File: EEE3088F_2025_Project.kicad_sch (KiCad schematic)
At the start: 1 part, among them U1 14528

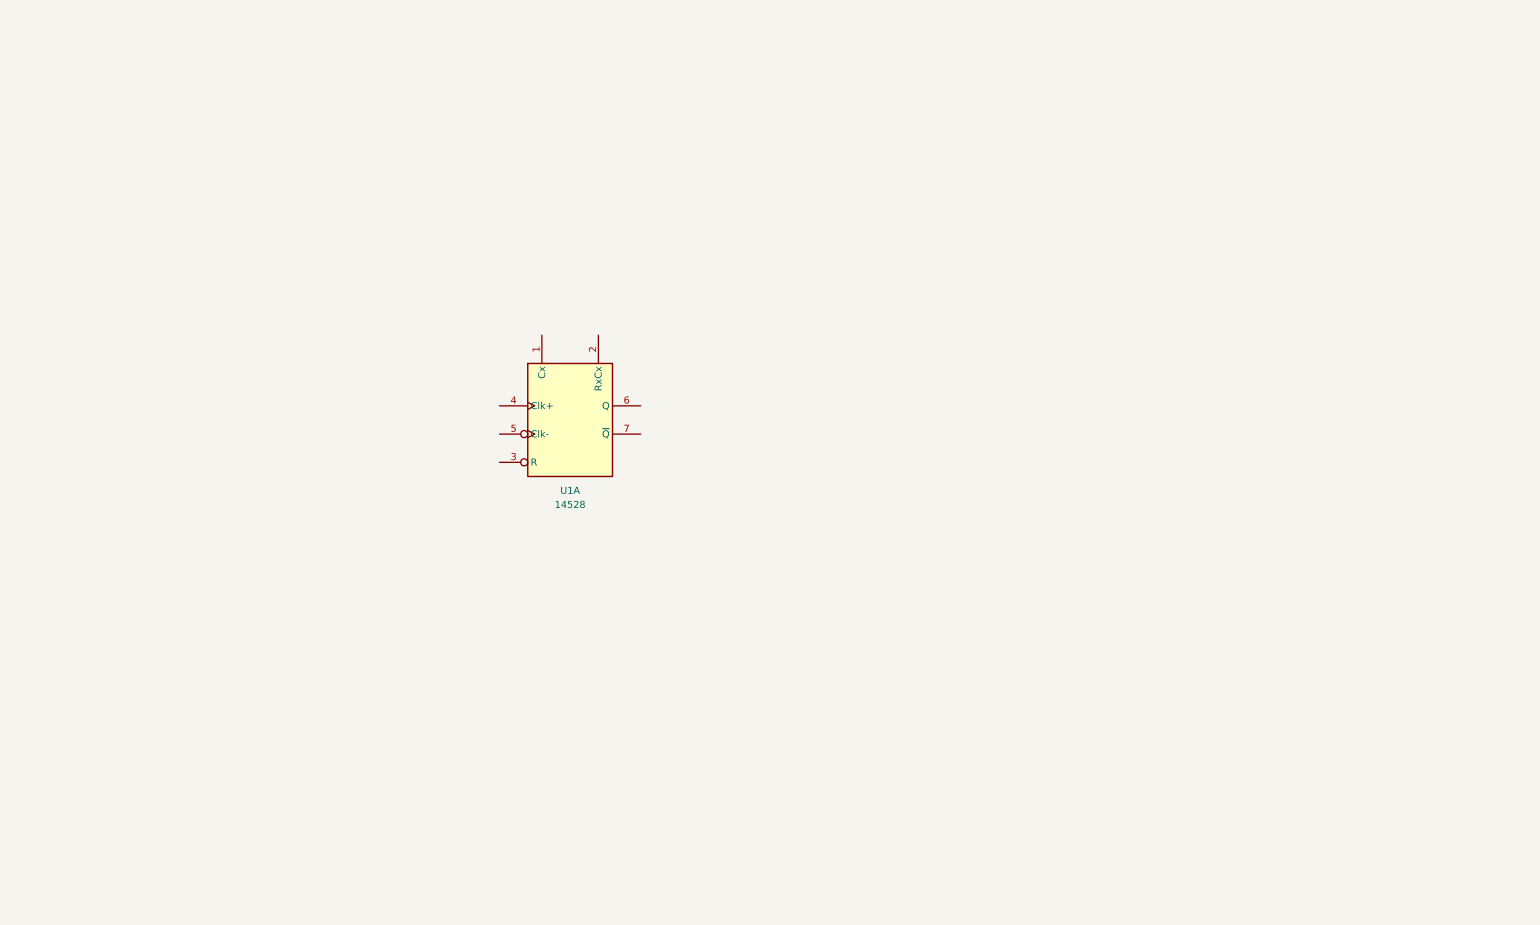
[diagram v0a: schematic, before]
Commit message: Addded motor drivers and connector
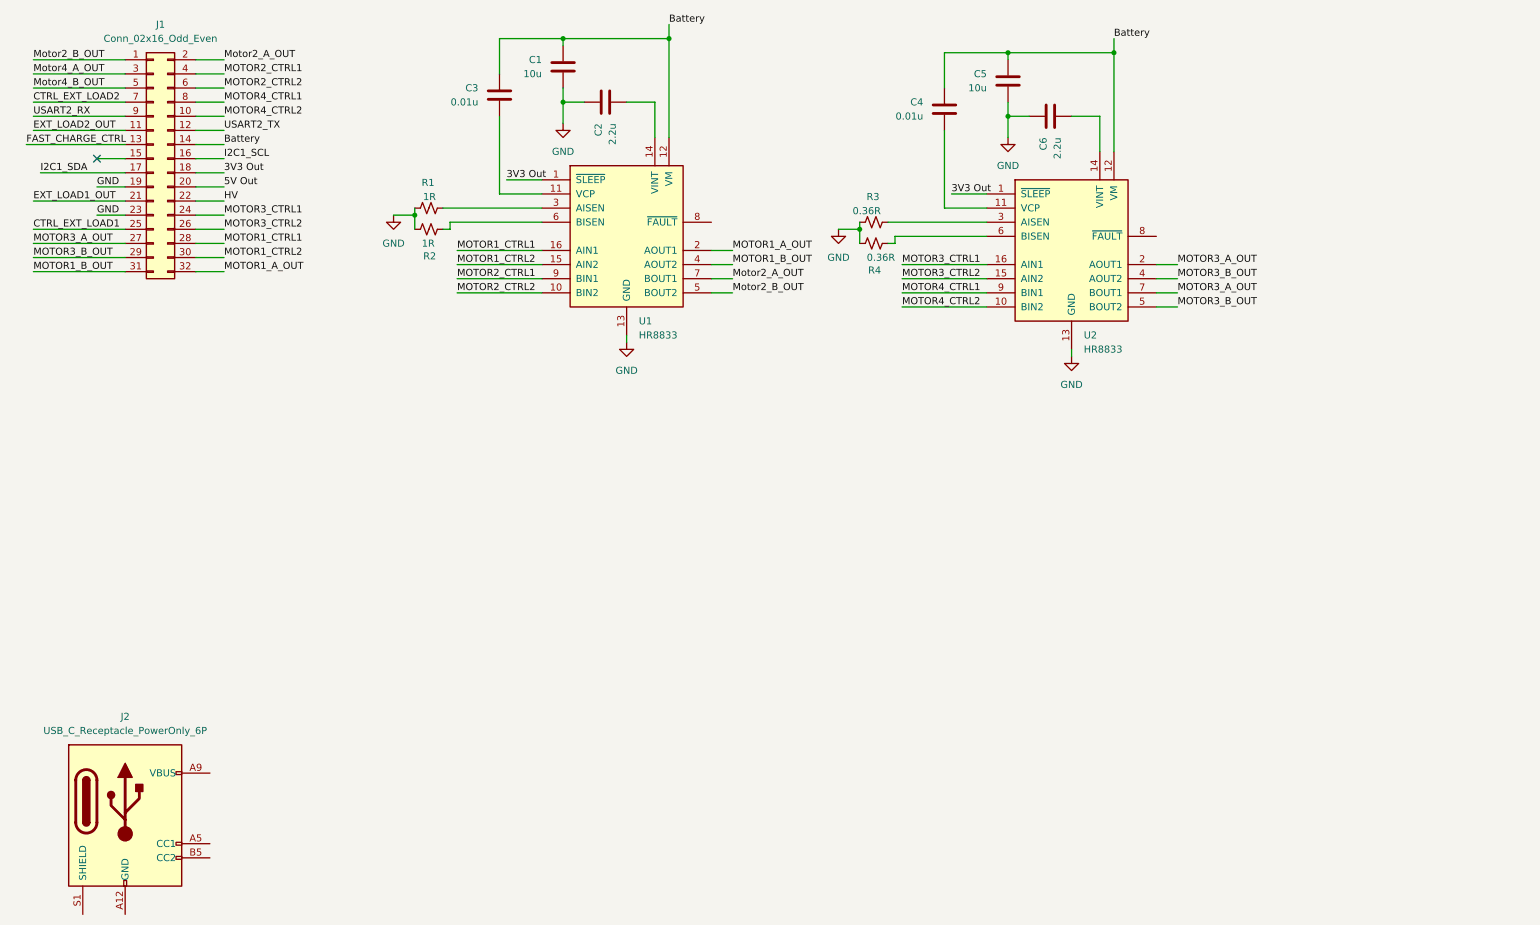
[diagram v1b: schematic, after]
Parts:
- removed U1: 14528, symbol 4xxx:14528
- added C1, C5: 10u, symbol Device:C
- added C2, C6: 2.2u, symbol Device:C
- added C3, C4: 0.01u, symbol Device:C
- added J1: Conn_02x16_Odd_Even, symbol Connector_Generic:Conn_02x16_Odd_Even
- added J2: USB_C_Receptacle_PowerOnly_6P, symbol Connector:USB_C_Receptacle_PowerOnly_6P
- added R1, R2: 1R, symbol Device:R_Small_US
- added R3, R4: 0.36R, symbol Device:R_Small_US
- added U1, U2: HR8833, Package_SO:TSSOP-16-1EP_4.4x5mm_P0.65mm_EP3x3mm, symbol Driver_Motor:DRV8833PW
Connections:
- new net: R2.2, U1.6 (BISEN)
- new net: C6.2, U2.14 (VINT)
- new net: J2.A12 (GND), J2.B12 (GND)
- new net: J2.A9 (VBUS), J2.B9 (VBUS)
- new net: C3.2, U1.11 (VCP)
- new net: C2.2, U1.14 (VINT)
- new net: R1.2, U1.3 (AISEN)
- new net: C4.2, U2.11 (VCP)
- new net: R3.2, U2.3 (AISEN)
- new net: R4.2, U2.6 (BISEN)
- new net 3V3 Out: J1.18 (Pin_18), U1.1 (~{SLEEP}), U2.1 (~{SLEEP})
- new net 5V Out: J1.20 (Pin_20)
- new net Battery: C1.1, C3.1, C4.1, C5.1, J1.14 (Pin_14), U1.12 (VM), U2.12 (VM)
- new net CTRL_EXT_LOAD1: J1.25 (Pin_25)
- new net CTRL_EXT_LOAD2: J1.7 (Pin_7)
- new net EXT_LOAD1_OUT: J1.21 (Pin_21)
- new net EXT_LOAD2_OUT: J1.11 (Pin_11)
- new net FAST_CHARGE_CTRL: J1.13 (Pin_13)
- new net GND: C1.2, C2.1, C5.2, C6.1, J1.19 (Pin_19), J1.23 (Pin_23), R1.1, R2.1, R3.1, R4.1, U1.13 (GND), U2.13 (GND)
- new net HV: J1.22 (Pin_22)
- new net I2C1_SCL: J1.16 (Pin_16)
- new net I2C1_SDA: J1.17 (Pin_17)
- new net MOTOR1_A_OUT: J1.32 (Pin_32), U1.2 (AOUT1)
- new net MOTOR1_B_OUT: J1.31 (Pin_31), U1.4 (AOUT2)
- new net MOTOR1_CTRL1: J1.28 (Pin_28), U1.16 (AIN1)
- new net MOTOR1_CTRL2: J1.30 (Pin_30), U1.15 (AIN2)
- new net MOTOR2_CTRL1: J1.4 (Pin_4), U1.9 (BIN1)
- new net MOTOR2_CTRL2: J1.6 (Pin_6), U1.10 (BIN2)
- new net MOTOR3_A_OUT: J1.27 (Pin_27), U2.2 (AOUT1), U2.7 (BOUT1)
- new net MOTOR3_B_OUT: J1.29 (Pin_29), U2.4 (AOUT2), U2.5 (BOUT2)
- new net MOTOR3_CTRL1: J1.24 (Pin_24), U2.16 (AIN1)
- new net MOTOR3_CTRL2: J1.26 (Pin_26), U2.15 (AIN2)
- new net MOTOR4_CTRL1: J1.8 (Pin_8), U2.9 (BIN1)
- new net MOTOR4_CTRL2: J1.10 (Pin_10), U2.10 (BIN2)
- new net Motor2_A_OUT: J1.2 (Pin_2), U1.7 (BOUT1)
- new net Motor2_B_OUT: J1.1 (Pin_1), U1.5 (BOUT2)
- new net Motor4_A_OUT: J1.3 (Pin_3)
- new net Motor4_B_OUT: J1.5 (Pin_5)
- new net USART2_RX: J1.9 (Pin_9)
- new net USART2_TX: J1.12 (Pin_12)
- no-connect marks 0 -> 1

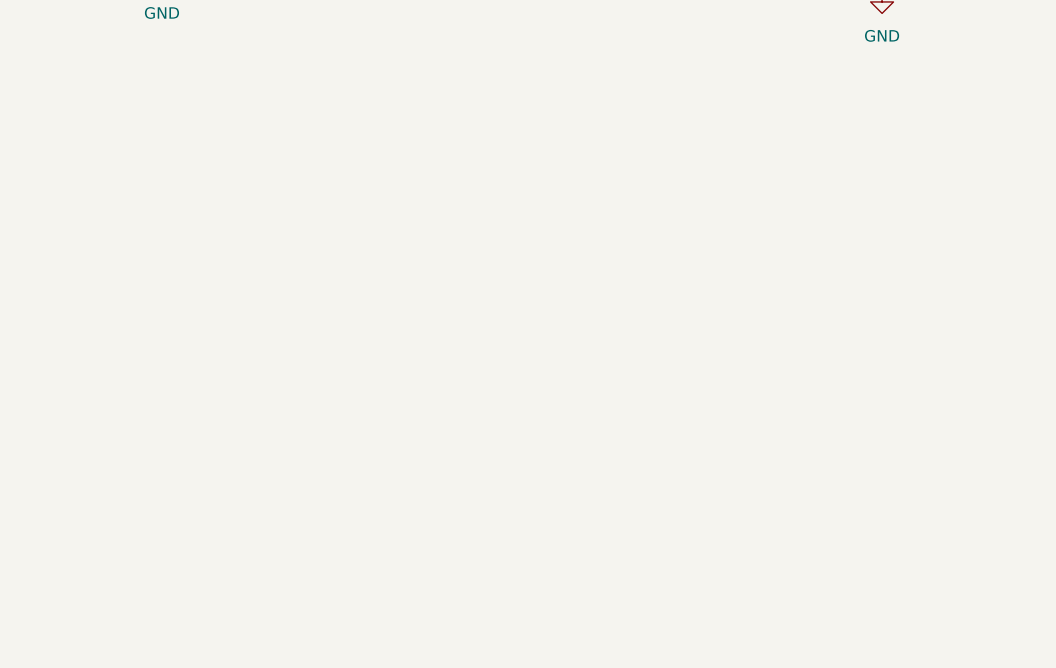
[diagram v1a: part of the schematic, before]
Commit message: Added dummy charging IC, struggling to add JLCPCB to Kicad
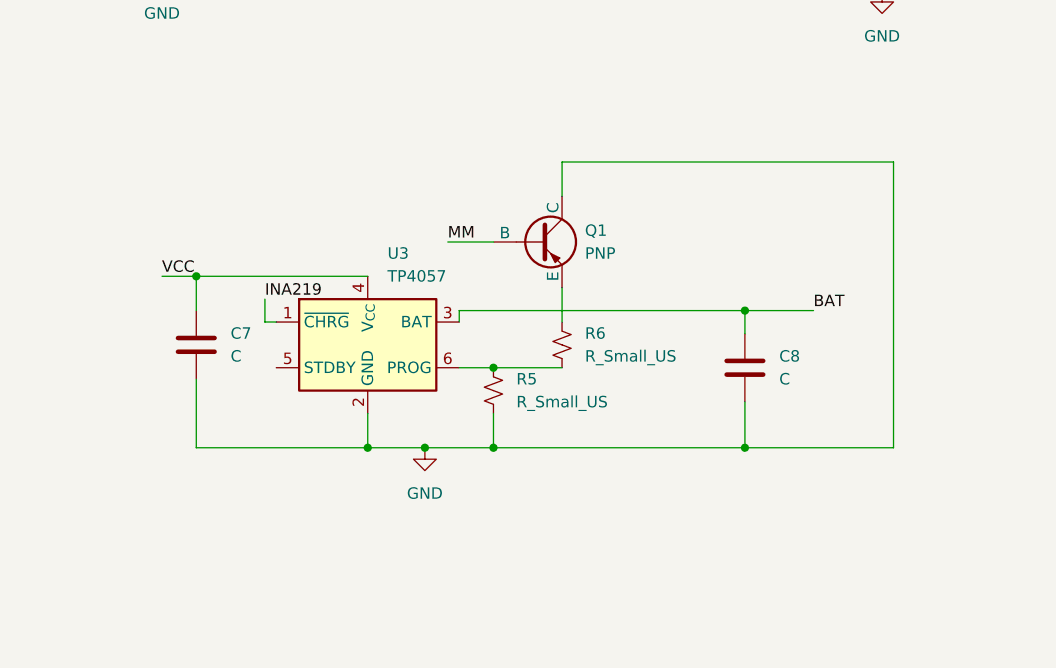
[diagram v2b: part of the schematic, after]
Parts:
- added C7, C8: C, symbol Device:C
- added Q1: PNP, symbol Simulation_SPICE:PNP
- added R5, R6: R_Small_US, symbol Device:R_Small_US
- added U3: TP4057, Package_TO_SOT_SMD:TSOT-23-6, symbol Battery_Management:TP4057
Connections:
- net GND: now also C7.2, C8.2, Q1.1 (C), R5.2, U3.2 (GND)
- new net: Q1.3 (E), R6.1
- new net: R5.1, R6.2, U3.6 (PROG)
- new net BAT: C8.1, U3.3 (BAT)
- new net INA219: U3.1 (~{CHRG})
- new net MM: Q1.2 (B)
- new net VCC: C7.1, U3.4 (V_{CC})

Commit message: Added dummy charging IC, struggling to add JLCPCB to Kicad
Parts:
- C7, C8: value C -> 1u
- R5: value R_Small_US -> 15K
- R6: value R_Small_US -> 1R6
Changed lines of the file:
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@@
 			)
 		)
-		(property "Value" "R_Small_US"
+		(property "Value" "1R6"
 			(at 170.18 116.8399 0)
 			(effects
@@
 			)
 		)
-		(property "Value" "R_Small_US"
+		(property "Value" "15K"
 			(at 162.56 121.9199 0)
 			(effects
@@
 			)
 		)
-		(property "Value" "C"
+		(property "Value" "1u"
 			(at 130.81 116.8399 0)
 			(effects
@@
 			)
 		)
-		(property "Value" "C"
+		(property "Value" "1u"
 			(at 191.77 119.3799 0)
 			(effects

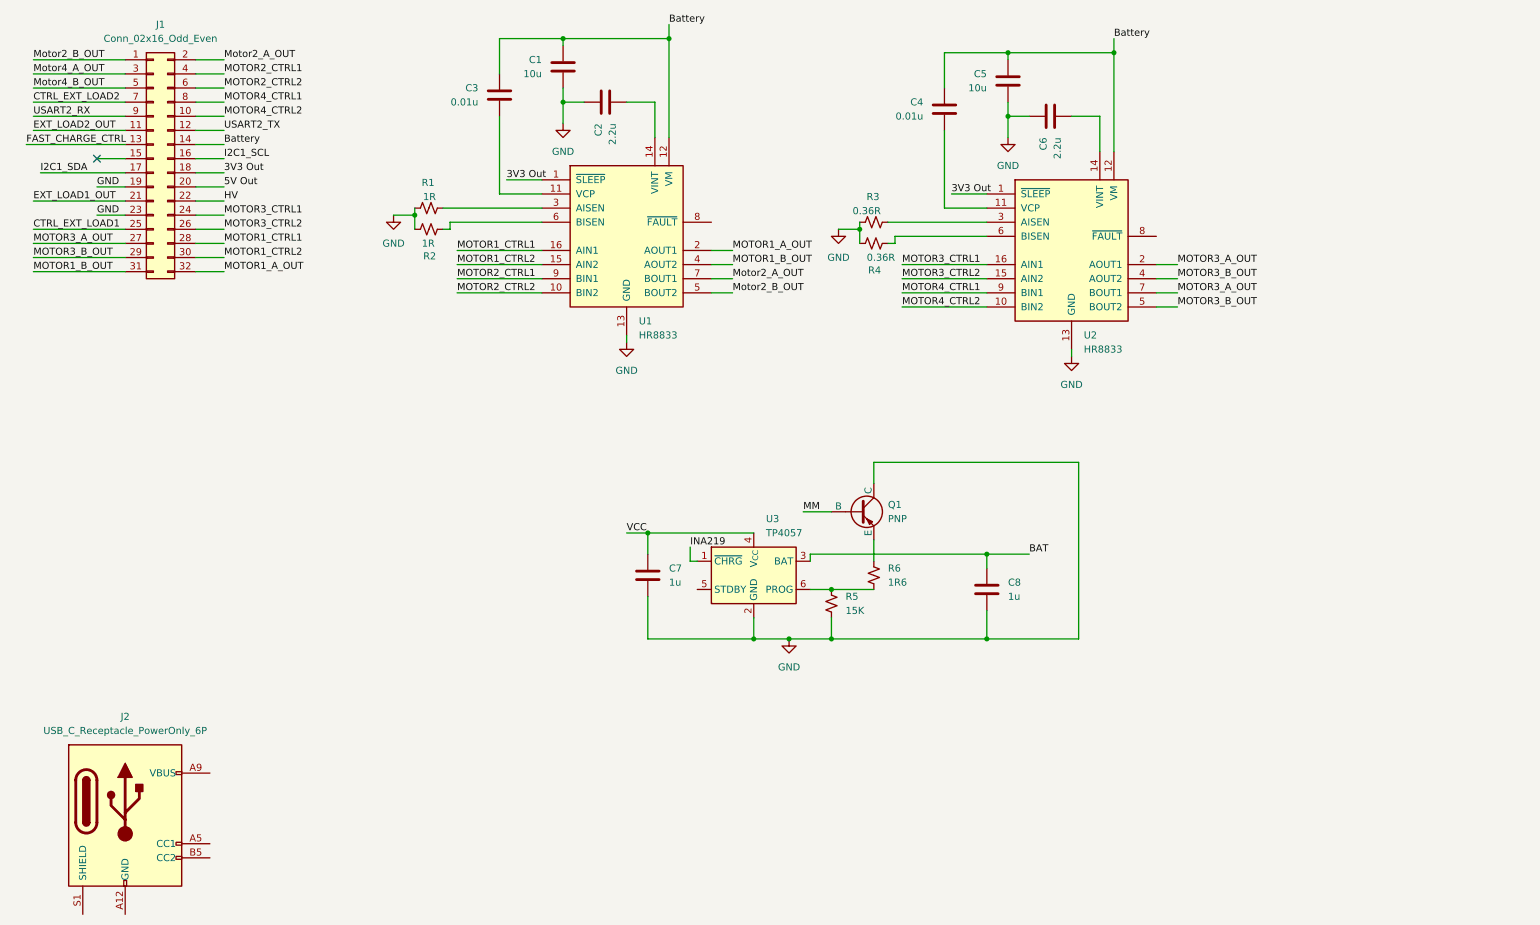
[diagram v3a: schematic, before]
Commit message: Added a switch, 3V3 and 5V out, intergrated USB C
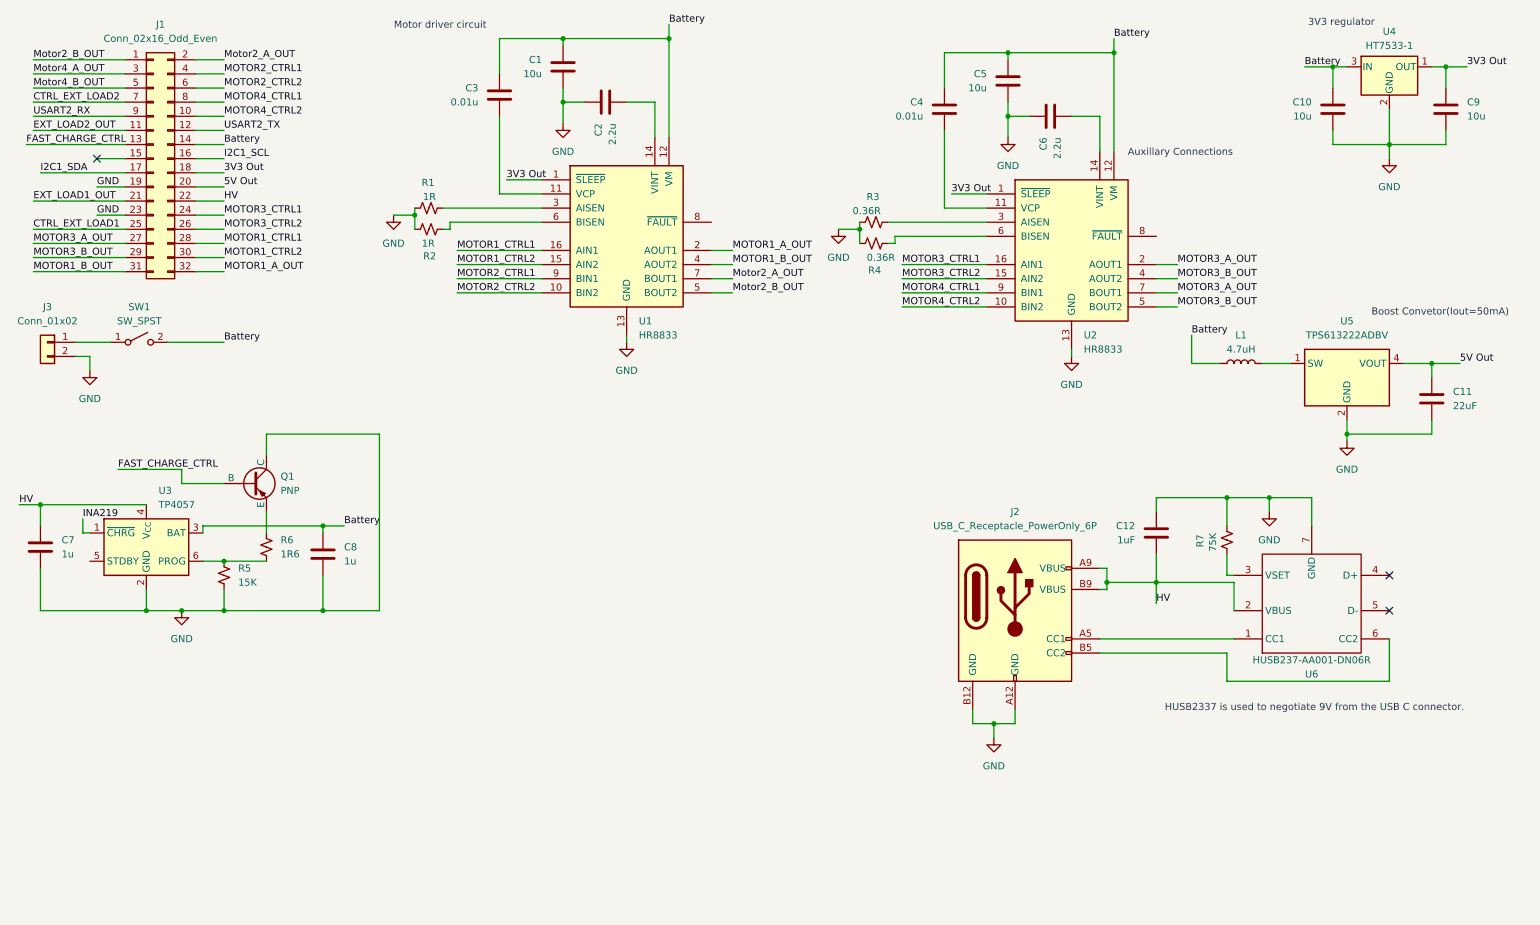
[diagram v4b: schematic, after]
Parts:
- added C10, C9: 10u, symbol Device:C
- added C11: 22uF, symbol Device:C
- added C12: 1uF, symbol Device:C
- added J3: Conn_01x02, symbol Connector_Generic:Conn_01x02
- added L1: 4.7uH, symbol Device:L
- added R7: 75K, symbol Device:R_Small_US
- added SW1: SW_SPST, symbol Switch:SW_SPST
- added U4: HT7533-1, Package_TO_SOT_SMD:SOT-89-3, symbol Regulator_Linear:L78L33_SOT89
- added U5: TPS613222ADBV, Package_TO_SOT_SMD:SOT-23-5, symbol Regulator_Switching:TPS613222ADBV
- added U6: HUSB237-AA001-DN06R, Package_DFN_QFN:DFN-6-1EP_2x2mm_P0.65mm_EP1.01x1.7mm, symbol MM symbols:HUSB237
- J2: footprint (none) -> Connector_USB:USB_C_Receptacle_GCT_USB4125-xx-x_6P_TopMnt_Horizontal; LCSC (none) -> C456012
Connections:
- net BAT is gone; now on net Battery: C8.1, U3.3 (BAT)
- net MM is gone; now on net FAST_CHARGE_CTRL: Q1.2 (B)
- net VCC is gone; now on net HV: C7.1, U3.4 (V_{CC})
- net 3V3 Out: now also C9.1, U4.1 (OUT)
- net 5V Out: now also C11.1, U5.4 (VOUT)
- net Battery: now also C10.1, L1.1, SW1.2 (B), U4.3 (IN)
- net GND: now also J2.A12 (GND), J2.B12 (GND), C10.2, C11.2, C12.1, C9.2, J3.2 (Pin_2), R7.1, U4.2 (GND), U5.2 (GND), U6.7 (GND)
- net HV: now also J2.A9 (VBUS), J2.B9 (VBUS), C12.2, U6.2 (VBUS)
- net at J2.A5 (CC1): now also U6.1 (CC1)
- net at J2.B5 (CC2): now also U6.6 (CC2)
- new net: R7.2, U6.3 (VSET)
- new net: L1.2, U5.1 (SW)
- new net: J3.1 (Pin_1), SW1.1 (A)
- no-connect marks 1 -> 3
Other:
- note added: "3V3 regulator"
- note added: "Auxillary Connections"
- note added: "Boost Convetor(Iout=50mA)"
- note added: "HUSB2337 is used to negotiate 9V from the USB C connector."
- note added: "Motor driver circuit"
- moved on the sheet: C7, C8, Q1, R5, R6, U3
